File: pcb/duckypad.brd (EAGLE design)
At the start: 110 x 96 mm, 157 parts, among them IC2 REG1117, SW1 SPST_TACT-EVQQ2, SW2 SPST_TACT-EVQQ2, SW21 EC12E_SW, SW22 EC12E_SW, SW3 324_SW324_SWITCH_FOOT_HOLE, SW4 324_SW324_SWITCH_FOOT_HOLE, U1 USBC_16P, U2 USBC_16P, U3 ESP32-S3FN8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

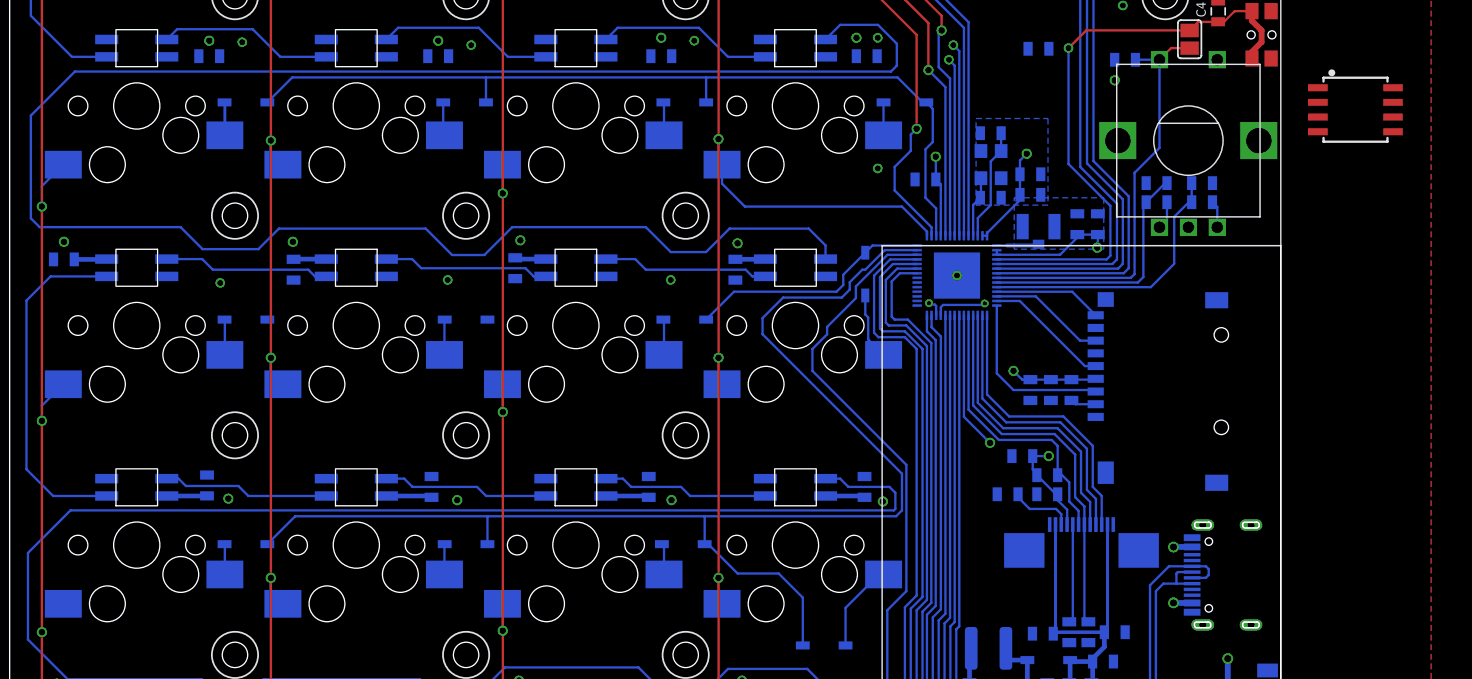
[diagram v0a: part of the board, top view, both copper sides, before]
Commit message: hooked up spi flash
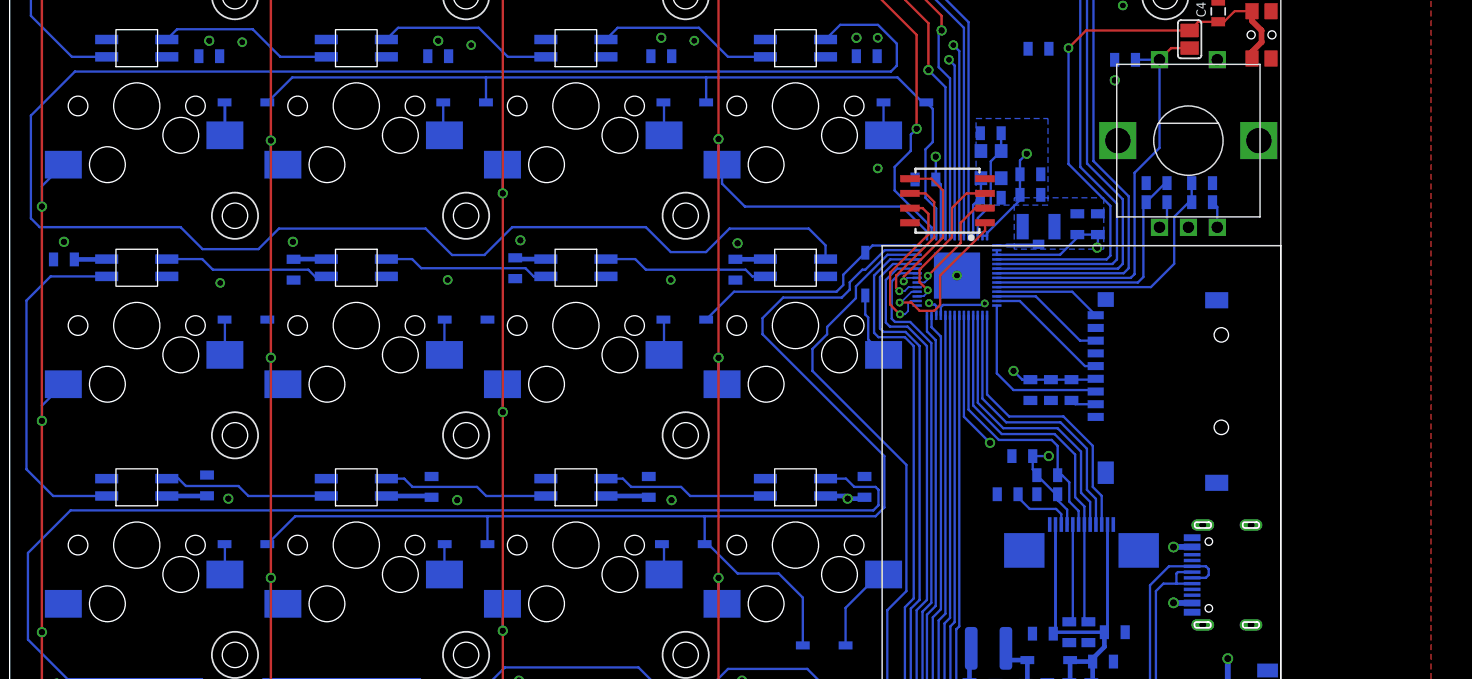
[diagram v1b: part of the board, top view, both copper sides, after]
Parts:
- moved U5 36.2 mm to (81.2, 58.8), turned to 90 degrees
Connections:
- new net N$74: U3.33, U5.6
- new net N$75: U3.30, U5.7
- new net N$76: U3.31, U5.3
- new net N$77: U3.32, U5.1
- new net N$78: U3.34, U5.2
- new net N$79: U3.35, U5.5
- net +3V3: now also U5.8
- net GND: now also U5.4
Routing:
- net N$77: track 0.00 -> 14.6 mm, vias 0 -> 1
- net N$75: track 0.00 -> 14.6 mm, vias 0 -> 1
- net N$79: track 0.00 -> 13.9 mm, vias 0 -> 1
- net N$74: track 0.00 -> 13.3 mm, vias 0 -> 1
- net N$76: track 0.00 -> 13.2 mm, vias 0 -> 1
- net N$78: track 0.00 -> 9.75 mm, vias 0 -> 1
- net N$20: track 167.7 -> 164.8 mm
- net ROW3: track 113.3 -> 111.0 mm
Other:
- board text added: "watch out for strapping pins GPIO3 must have pull resistor, pull to high to free up JTAG pins? 3.5mm corner radius"
- board text removed: "watch out for strapping pins GPIO3 must have pull resistor, pull to high to free up JTAG pins? 3.5mm corner radius MOVED: MOSI SCLK MISO CARD_DET OLED_RESET (new)"

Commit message: led power
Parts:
- added C30: 1uF, clock:0805
- added C32: 100nF, clock:0805
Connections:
- net +3V3: now also C30.2, C32.2
- net GND: now also C30.1, C32.1
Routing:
- net +3V3: track 131.9 -> 184.7 mm, vias 31 -> 32
- net GND: track 31.5 -> 52.3 mm, vias 19 -> 20
- net ROW0: track 94.4 -> 93.7 mm

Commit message: working on new PCB
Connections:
- removed net N$66: U3.28, X3.5
- net GND: now also X3.5
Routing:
- net N$66: track 66.4 -> 0.00 mm
- net ROW2: track 21.4 -> 64.2 mm
- net N$28: track 73.3 -> 78.3 mm
- net +3V3: track 184.7 -> 188.7 mm, vias 32 -> 33
- net COL0: track 203.7 -> 207.0 mm
- net RESET: track 51.4 -> 53.1 mm
- net N$67: track 74.3 -> 73.5 mm

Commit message: finishing touches
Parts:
- removed X3: SM12B-SSR-H-TB, duckypad:SM12B-SSR-H-TB
- added U$3: SH10P, duckypad:DUCKYPAD_SM12B-SSR-H-TB
- D1, D10, D11, D12, D13, D14, D15, D16, D17, D18, D19, D2, D20, D21, D3, D4, D5, D6, D7, D8, D9: device adafruit_changed:SOD-123 -> duckypad:ADAFRUIT_CHANGED_SOD-123
- moved JP3 0.57 mm to (107.4, 2.16)
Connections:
- net +3V3: now also U$3.3; no longer X3.3
- net GND: now also U$3.2, U$3.FIT@1, U$3.FIT@2; no longer X3.12, X3.2, X3.5, X3.FIT@1, X3.FIT@2
- net N$1: now also U$3.1; no longer X3.1
- net N$37: now also U$3.4; no longer X3.4
- net N$67: now also U$3.5; no longer X3.6
- net N$68: now also U$3.6; no longer X3.7
- net N$69: now also U$3.7; no longer X3.8
- net N$70: now also U$3.8; no longer X3.9
- net N$72: now also U$3.9; no longer X3.10
- net N$73: now also U$3.10; no longer X3.11
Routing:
- net GND: track 52.3 -> 46.6 mm
- net N$68: track 79.5 -> 75.3 mm
- net N$69: track 81.1 -> 80.5 mm
- net N$72: track 108.8 -> 109.4 mm
- net N$73: track 115.6 -> 115.1 mm

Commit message: finishing touches
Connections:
- removed net N$32: C29.2, IC2.3, JP2.2
- new net N$66: C29.2, IC2.3, JP2.2, U$3.1, U1.A4B9, U1.B4A9
- net N$1: no longer U$3.1, U1.A4B9, U1.B4A9
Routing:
- net N$66: track 0.00 -> 117.3 mm, vias 0 -> 1
- net N$1: track 100.8 -> 17.3 mm, vias 4 -> 0
- net N$32: track 13.1 -> 0.00 mm
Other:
- board text added: "watch out for strapping pins GPIO3 must have pull resistor, pull to high to free up JTAG pins? 3.5mm corner radius double check RESET jumper has NO PASTE"
- board text removed: "watch out for strapping pins GPIO3 must have pull resistor, pull to high to free up JTAG pins? 3.5mm corner radius"

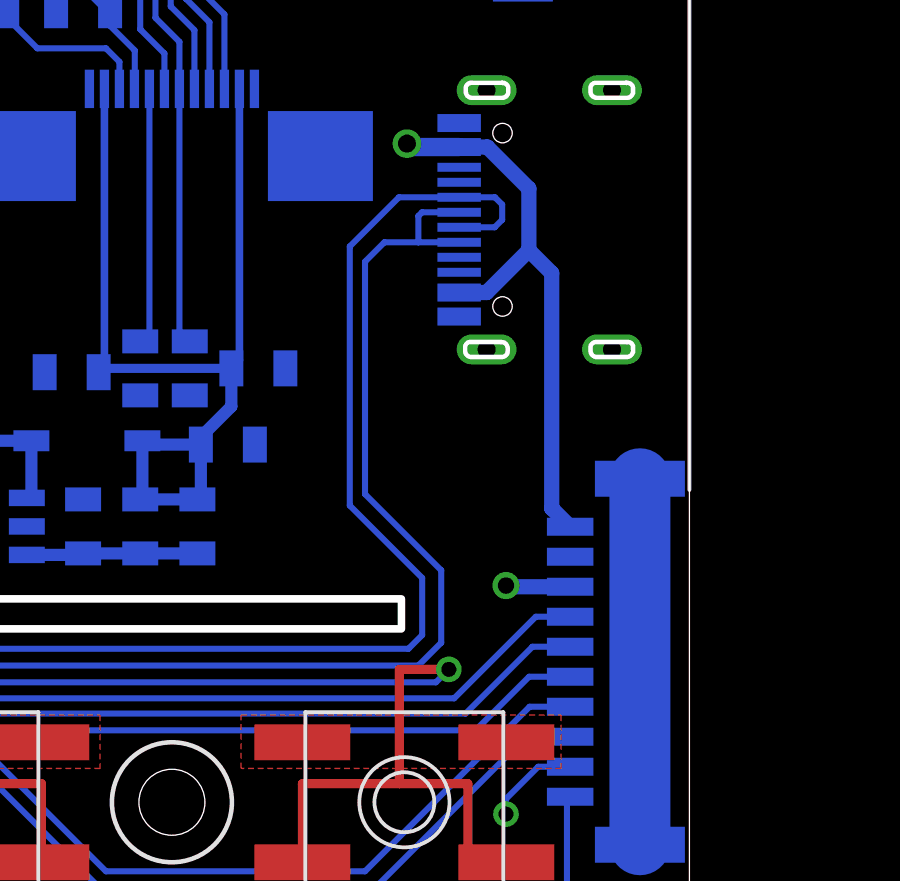
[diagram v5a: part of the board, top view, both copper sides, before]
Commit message: wired up CC pins
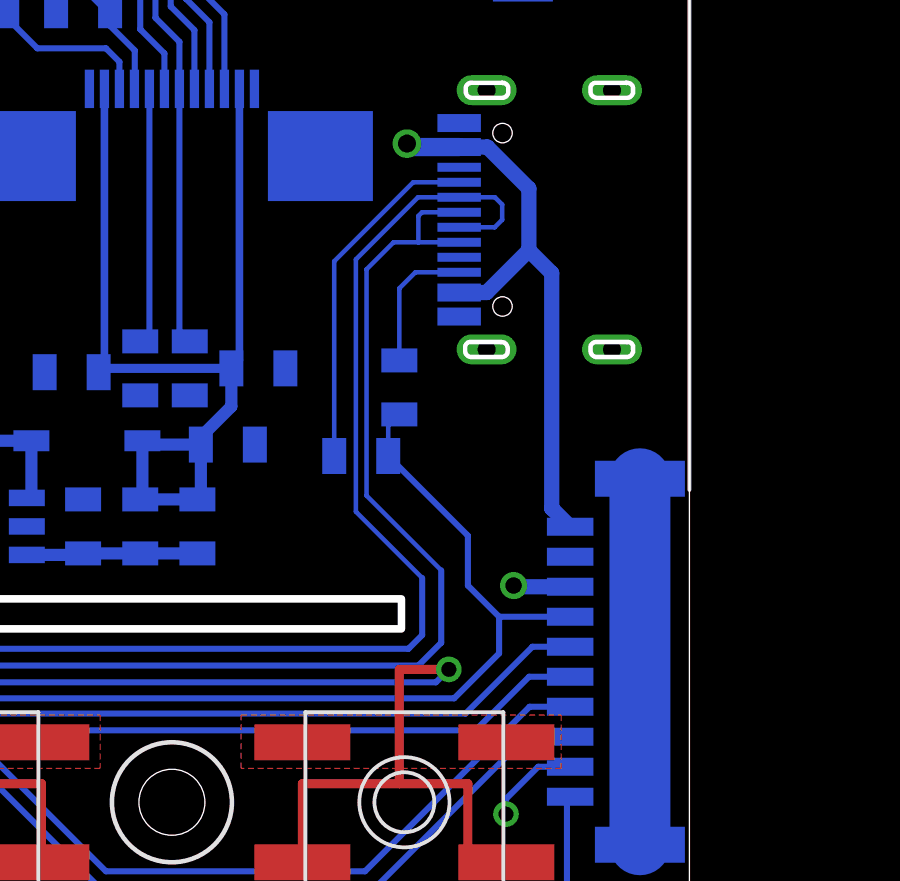
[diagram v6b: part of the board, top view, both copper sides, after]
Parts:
- added R18, R4: 470, joyAnalog:0805
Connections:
- removed net N$37: U$3.4, U3.27
- new net CC_BUSY: R18.1, R4.1, U$3.4, U3.27
- new net N$32: R4.2, U1.A5
- new net N$80: R18.2, U1.B5
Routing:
- net CC_BUSY: track 0.00 -> 74.6 mm
- net N$37: track 65.4 -> 0.00 mm
- net N$32: track 0.00 -> 11.7 mm
- net N$80: track 0.00 -> 4.62 mm
- net AUX_DN: track 77.0 -> 76.5 mm
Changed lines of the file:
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@@
 </element>
 <element name="U$3" library="duckypad" package="DUCKYPAD_SM12B-SSR-H-TB" value="SH10P" x="107.95" y="11.684" smashed="yes" rot="MR270"/>
+<element name="R4" library="joyAnalog" package="0805" value="470" x="99.06" y="18.542" smashed="yes" rot="MR0">
+<attribute name="NAME" x="99.822" y="19.3675" size="0.8128" layer="26" rot="MR0"/>
+</element>
+<element name="R18" library="joyAnalog" package="0805" value="470" x="100.33" y="20.828" smashed="yes" rot="MR90">
+<attribute name="NAME" x="101.1555" y="20.066" size="0.8128" layer="26" rot="MR90"/>
+</element>
 </elements>
 <signals>
@@
 <wire x1="88.066" y1="72.009" x2="88.127" y2="71.948" width="0.2032" layer="16"/>
 <contactref element="U$3" pad="3"/>
-<via x="103.886" y="14.224" extent="1-16" drill="0.55"/>
-<wire x1="106.025" y1="14.184" x2="103.926" y2="14.184" width="0.508" layer="16"/>
-<wire x1="103.926" y1="14.184" x2="103.886" y2="14.224" width="0.508" layer="16"/>
+<via x="104.14" y="14.224" extent="1-16" drill="0.55"/>
+<wire x1="106.025" y1="14.184" x2="104.18" y2="14.184" width="0.508" layer="16"/>
+<wire x1="104.18" y1="14.184" x2="104.14" y2="14.224" width="0.508" layer="16"/>
 <wire x1="87.9746" y1="83.6496" x2="87.9746" y2="77.3758" width="1.016" layer="1"/>
 <wire x1="87.9746" y1="77.3758" x2="88" y2="77.3504" width="1.016" layer="1"/>
@@
 <contactref element="U1" pad="B6"/>
 <contactref element="U1" pad="A6"/>
-<wire x1="102.3245" y1="26.666" x2="101.088" y2="26.666" width="0.2032" layer="16"/>
-<wire x1="101.088" y1="26.666" x2="100.965" y2="26.543" width="0.2032" layer="16"/>
-<wire x1="100.965" y1="25.666" x2="102.3245" y2="25.666" width="0.2032" layer="16"/>
-<wire x1="100.965" y1="26.543" x2="100.965" y2="25.666" width="0.2032" layer="16"/>
+<wire x1="102.3245" y1="26.666" x2="101.088" y2="26.666" width="0.1524" layer="16"/>
+<wire x1="101.088" y1="26.666" x2="100.965" y2="26.543" width="0.1524" layer="16"/>
+<wire x1="100.965" y1="25.666" x2="102.3245" y2="25.666" width="0.1524" layer="16"/>
+<wire x1="100.965" y1="26.543" x2="100.965" y2="25.666" width="0.1524" layer="16"/>
 <contactref element="U3" pad="22"/>
 <wire x1="81.407" y1="21.971" x2="81.407" y2="13.716" width="0.2032" layer="16"/>
 <wire x1="83.566" y1="11.557" x2="100.965" y2="11.557" width="0.2032" layer="16"/>
 <wire x1="100.965" y1="11.557" x2="101.727" y2="12.319" width="0.2032" layer="16"/>
-<wire x1="101.727" y1="14.732" x2="99.187" y2="17.272" width="0.2032" layer="16"/>
-<wire x1="99.187" y1="17.272" x2="99.187" y2="25.019" width="0.2032" layer="16"/>
-<wire x1="99.834" y1="25.666" x2="100.965" y2="25.666" width="0.2032" layer="16"/>
+<wire x1="101.727" y1="14.732" x2="99.2378" y2="17.2212" width="0.1524" layer="16"/>
+<wire x1="100.1388" y1="25.666" x2="100.965" y2="25.666" width="0.1524" layer="16"/>
 <wire x1="81.407" y1="13.716" x2="83.566" y2="11.557" width="0.2032" layer="16"/>
 <wire x1="101.727" y1="12.319" x2="101.727" y2="14.732" width="0.2032" layer="16"/>
-<wire x1="99.187" y1="25.019" x2="99.834" y2="25.666" width="0.2032" layer="16"/>
+<wire x1="99.2378" y1="24.765" x2="100.1388" y2="25.666" width="0.1524" layer="16"/>
 <wire x1="81.776" y1="48.879" x2="81.776" y2="22.34" width="0.2032" layer="16"/>
 <wire x1="81.776" y1="22.34" x2="81.407" y2="21.971" width="0.2032" layer="16"/>
+<wire x1="99.2378" y1="24.765" x2="99.2378" y2="17.2212" width="0.1524" layer="16"/>
 </signal>
 <signal name="AUX_DN">
 <contactref element="U1" pad="B7"/>
 <contactref element="U1" pad="A7"/>
-<wire x1="102.3245" y1="27.166" x2="103.517" y2="27.166" width="0.2032" layer="16"/>
-<wire x1="103.517" y1="27.166" x2="103.759" y2="26.924" width="0.2032" layer="16"/>
-<wire x1="103.759" y1="26.924" x2="103.759" y2="26.416" width="0.2032" layer="16"/>
-<wire x1="103.509" y1="26.166" x2="102.3245" y2="26.166" width="0.2032" layer="16"/>
-<wire x1="103.759" y1="26.416" x2="103.509" y2="26.166" width="0.2032" layer="16"/>
+<wire x1="102.3245" y1="27.166" x2="103.517" y2="27.166" width="0.1524" layer="16"/>
+<wire x1="103.517" y1="27.166" x2="103.759" y2="26.924" width="0.1524" layer="16"/>
+<wire x1="103.759" y1="26.924" x2="103.759" y2="26.416" width="0.1524" layer="16"/>
+<wire x1="103.509" y1="26.166" x2="102.3245" y2="26.166" width="0.1524" layer="16"/>
+<wire x1="103.759" y1="26.416" x2="103.509" y2="26.166" width="0.1524" layer="16"/>
 <contactref element="U3" pad="21"/>
 <wire x1="81.915" y1="13.97" x2="83.7692" y2="12.1158" width="0.2032" layer="16"/>
@@
 <wire x1="100.6348" y1="12.1158" x2="101.092" y2="12.573" width="0.2032" layer="16"/>
 <wire x1="101.092" y1="12.573" x2="101.092" y2="14.478" width="0.2032" layer="16"/>
-<wire x1="101.092" y1="14.478" x2="98.679" y2="16.891" width="0.2032" layer="16"/>
-<wire x1="98.679" y1="16.891" x2="98.679" y2="25.527" width="0.2032" layer="16"/>
-<wire x1="100.318" y1="27.166" x2="102.3245" y2="27.166" width="0.2032" layer="16"/>
+<wire x1="98.8822" y1="16.6878" x2="101.092" y2="14.478" width="0.1524" layer="16"/>
 <wire x1="81.915" y1="21.717" x2="81.915" y2="13.97" width="0.2032" layer="16"/>
-<wire x1="98.679" y1="25.527" x2="100.318" y2="27.166" width="0.2032" layer="16"/>
 <wire x1="82.176" y1="48.879" x2="82.176" y2="21.978" width="0.2032" layer="16"/>
 <wire x1="82.176" y1="21.978" x2="81.915" y2="21.717" width="0.2032" layer="16"/>
+<wire x1="102.3245" y1="27.166" x2="100.953" y2="27.166" width="0.1524" layer="16"/>
+<wire x1="100.953" y1="27.166" x2="98.8822" y2="25.0952" width="0.1524" layer="16"/>
+<wire x1="98.8822" y1="25.0952" x2="98.8822" y2="16.6878" width="0.1524" layer="16"/>
 </signal>
 <signal name="N$28">
@@
 <wire x1="84.836" y1="11.303" x2="84.836" y2="7.62" width="0.3048" layer="1"/>
 </signal>
-<signal name="N$37">
+<signal name="CC_BUSY">
 <contactref element="U3" pad="27"/>
 <wire x1="79.776" y1="48.879" x2="79.776" y2="47.732" width="0.2032" layer="16"/>
@@
 <wire x1="81.1022" y1="10.4648" x2="102.1588" y2="10.4648" width="0.2032" layer="16"/>
 <contactref element="U$3" pad="4"/>
-<wire x1="102.1588" y1="10.4648" x2="104.878" y2="13.184" width="0.2032" layer="16"/>
-<wire x1="104.878" y1="13.184" x2="106.025" y2="13.184" width="0.2032" layer="16"/>
+<contactref element="R4" pad="1"/>
+<contactref element="R18" pad="1"/>
+<wire x1="100.33" y1="19.928" x2="99.96" y2="19.558" width="0.1524" layer="16"/>
+<wire x1="99.96" y1="19.558" x2="99.96" y2="18.542" width="0.1524" layer="16"/>
+<wire x1="99.96" y1="18.542" x2="102.616" y2="15.886" width="0.2032" layer="16"/>
+<wire x1="102.616" y1="15.886" x2="102.616" y2="14.224" width="0.2032" layer="16"/>
+<wire x1="102.616" y1="14.224" x2="103.656" y2="13.184" width="0.2032" layer="16"/>
+<wire x1="103.656" y1="13.184" x2="106.025" y2="13.184" width="0.2032" layer="16"/>
+<wire x1="102.1588" y1="10.4648" x2="103.656" y2="11.962" width="0.2032" layer="16"/>
+<wire x1="103.656" y1="11.962" x2="103.656" y2="13.184" width="0.2032" layer="16"/>
 </signal>
 <signal name="N$67">
@@
 <wire x1="105.41" y1="16.799" x2="105.41" y2="24.638" width="0.508" layer="16"/>
 </signal>
+<signal name="N$32">
+<contactref element="R4" pad="2"/>
+<contactref element="U1" pad="A5"/>
+<wire x1="102.3245" y1="27.666" x2="100.7926" y2="27.666" width="0.1524" layer="16"/>
+<wire x1="98.16" y1="25.0334" x2="98.16" y2="18.542" width="0.1524" layer="16"/>
+<wire x1="100.7926" y1="27.666" x2="98.16" y2="25.0334" width="0.1524" layer="16"/>
+</signal>
+<signal name="N$80">
+<contactref element="R18" pad="2"/>
+<contactref element="U1" pad="B5"/>
+<wire x1="102.3245" y1="24.666" x2="100.866" y2="24.666" width="0.1524" layer="16"/>
+<wire x1="100.33" y1="24.13" x2="100.33" y2="21.728" width="0.1524" layer="16"/>
+<wire x1="100.866" y1="24.666" x2="100.33" y2="24.13" width="0.1524" layer="16"/>
+</signal>
 </signals>
